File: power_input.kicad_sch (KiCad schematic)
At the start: 8 parts, among them J1 DC005-T20, U1 DCDC Converter

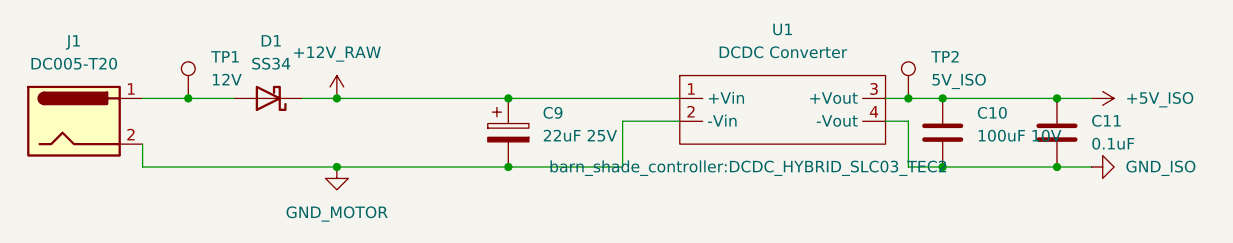
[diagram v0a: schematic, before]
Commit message: Pre-fab QA review fixes: switch input levels, power path, sensor spec, ESD
- R1-R8 switch series resistors 10k -> 1k: with only the ESP32 internal
  ~45k pull-up, 10k divided a closed switch to 0.6V vs the S3's 0.825V
  VIL limit — marginal. 1k gives ~0.1-0.23V worst case.
- U11 ACS723 -> ACS725LLCTR-05AB-T (C3684552): ACS723 needs 4.5-5.5V but
  ran at 3.3V (out of spec). ACS725 is 3.3V-native, same SOIC-8, rated
  to +150C. Firmware: sensitivity 264mV/A, formula (x-1.65)/0.264.
- D2 BAT54C (200mA) removed; replaced with D10/D11 SS34 (3A) diode-OR.
  The old diode carried the full ESP32 load permanently; WiFi TX bursts
  reach 350-500mA.
- U16 PRTR5V0U2X added on USB D+/D- (ESD protection at J2).
- D1 SS34 -> SS54 (5A, same SMA footprint) for multi-motor headroom.
- C10 bumped to 25V-rated 100uF 1210 (C2840614), same footprint.
- Filled all missing LCSC fields for JLCPCB assembly BOM.
- Docs: J4 pinout corrected to as-built; firmware bring-up checklist and
  RTS/DTR terminal gotcha added; CLAUDE.md placement guide for D10/D11/U16.

PCB placement of D10/D11/U16 + F8 sync still pending.

Co-Authored-By: Claude Fable 5 <noreply@anthropic.com>
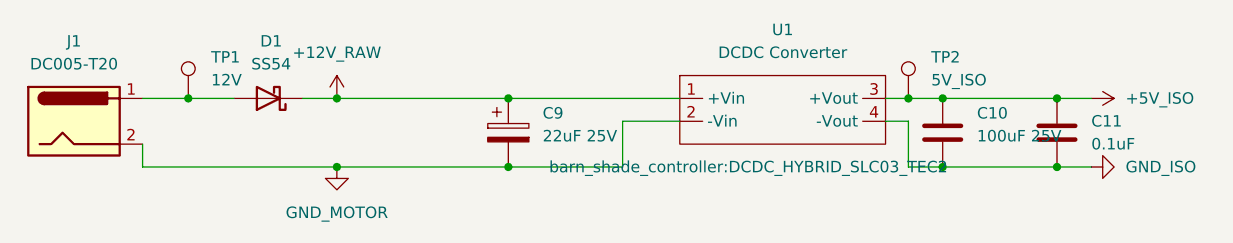
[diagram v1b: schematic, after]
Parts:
- C10: value 100uF 10V -> 100uF 25V; LCSC (none) -> C2840614
- D1: value SS34 -> SS54; LCSC C8678 -> C22452
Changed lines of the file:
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@@
 			)
 		)
-		(property "Value" "SS34"
+		(property "Value" "SS54"
 			(at 98.1075 71.12 0)
 			(show_name no)
@@
 			)
 		)
-		(property "Datasheet" "https://www.vishay.com/docs/88751/ss32.pdf"
+		(property "Datasheet" "https://www.lcsc.com/datasheet/lcsc_datasheet_1810192041_MDD-Microdiode-Electronics-SS54_C22452.pdf"
 			(at 97.79 74.93 0)
 			(hide yes)
@@
 			)
 		)
-		(property "LCSC" "C8678"
+		(property "LCSC" "C22452"
 			(at 97.79 74.93 0)
 			(hide yes)
@@
 			)
 		)
-		(property "Value" "100uF 10V"
+		(property "Value" "100uF 25V"
 			(at 176.53 79.1209 0)
 			(show_name no)
@@
 			)
 		)
-		(property "LCSC" ""
+		(property "LCSC" "C2840614"
 			(at 172.72 78.74 0)
 			(hide yes)
